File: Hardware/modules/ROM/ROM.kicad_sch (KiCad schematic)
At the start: 10 parts, among them J1 Bus_PCI_6502, U1 74HC138, U2 SST39SF040, U3 74HC00, U4 AS6C4008-55PCN

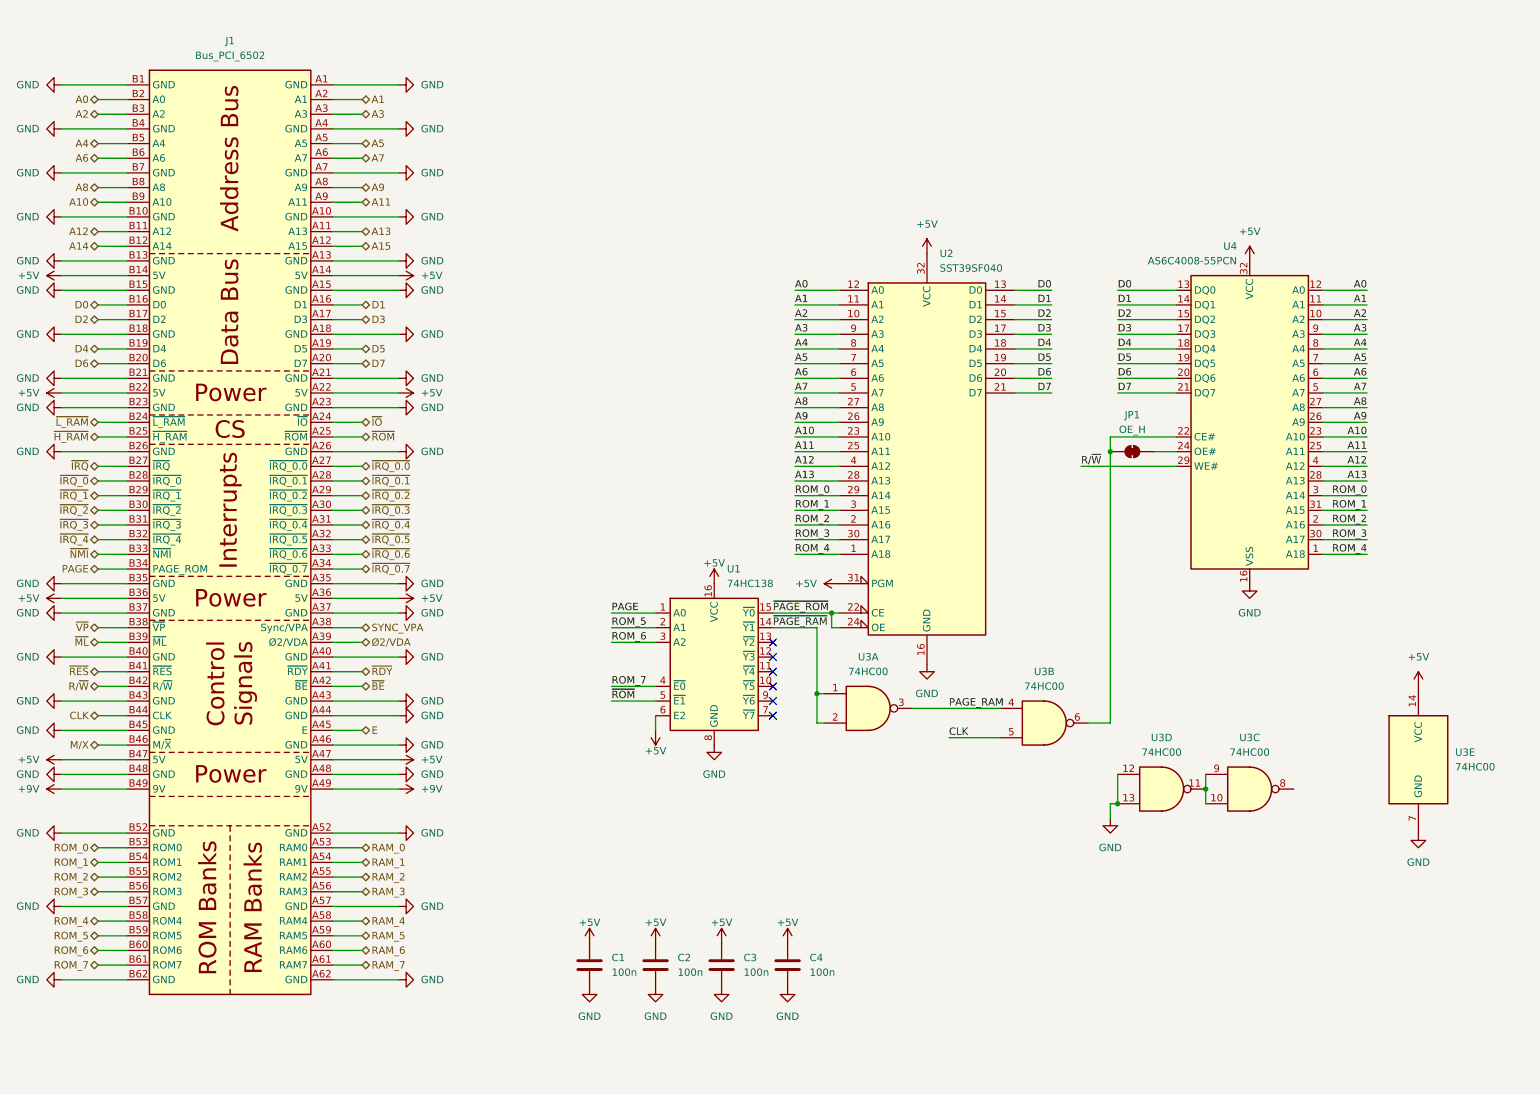
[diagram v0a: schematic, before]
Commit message: Hardware Update Add MyCPU VGA Module Beautify all Schematics minor Error corrections Readme Update
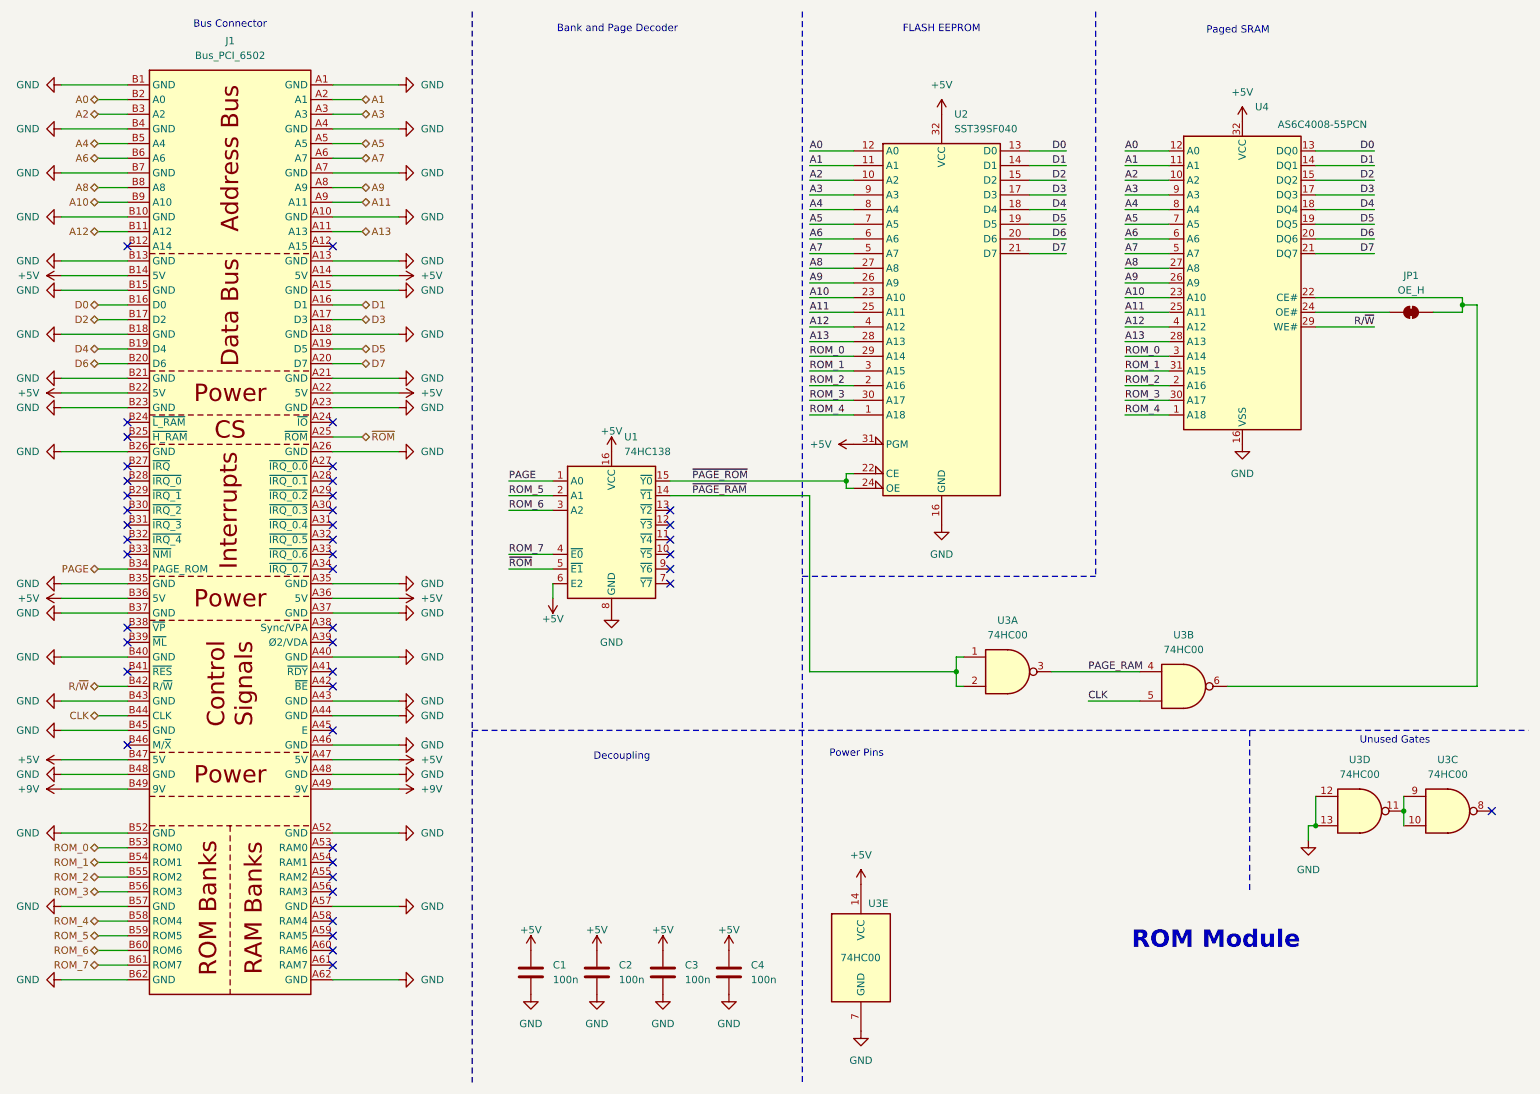
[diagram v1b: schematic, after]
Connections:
- net A14: no longer names the net of J1.B12 (A14)
- net A15: no longer names the net of J1.A12 (A15)
- net E: no longer names the net of J1.A45 (E)
- net M/X: no longer names the net of J1.B46 (M/~{X})
- net RAM_0: no longer names the net of J1.A53 (RAM0)
- net RAM_1: no longer names the net of J1.A54 (RAM1)
- net RAM_2: no longer names the net of J1.A55 (RAM2)
- net RAM_3: no longer names the net of J1.A56 (RAM3)
- net RAM_4: no longer names the net of J1.A58 (RAM4)
- net RAM_5: no longer names the net of J1.A59 (RAM5)
- net RAM_6: no longer names the net of J1.A60 (RAM6)
- net RAM_7: no longer names the net of J1.A61 (RAM7)
- net SYNC_VPA: no longer names the net of J1.A38 (Sync/VPA)
- net ~{BE}: no longer names the net of J1.A42 (~{BE})
- net ~{H_RAM}: no longer names the net of J1.B25 (~{H_RAM})
- net ~{IO}: no longer names the net of J1.A24 (~{IO})
- net ~{IRQ_0.0}: no longer names the net of J1.A27 (~{IRQ_0.0})
- net ~{IRQ_0.1}: no longer names the net of J1.A28 (~{IRQ_0.1})
- net ~{IRQ_0.2}: no longer names the net of J1.A29 (~{IRQ_0.2})
- net ~{IRQ_0.3}: no longer names the net of J1.A30 (~{IRQ_0.3})
- net ~{IRQ_0.4}: no longer names the net of J1.A31 (~{IRQ_0.4})
- net ~{IRQ_0.5}: no longer names the net of J1.A32 (~{IRQ_0.5})
- net ~{IRQ_0.6}: no longer names the net of J1.A33 (~{IRQ_0.6})
- net ~{IRQ_0.7}: no longer names the net of J1.A34 (~{IRQ_0.7})
- net ~{IRQ_0}: no longer names the net of J1.B28 (~{IRQ_0})
- net ~{IRQ_1}: no longer names the net of J1.B29 (~{IRQ_1})
- net ~{IRQ_2}: no longer names the net of J1.B30 (~{IRQ_2})
- net ~{IRQ_3}: no longer names the net of J1.B31 (~{IRQ_3})
- net ~{IRQ_4}: no longer names the net of J1.B32 (~{IRQ_4})
- net ~{IRQ}: no longer names the net of J1.B27 (~{IRQ})
- net ~{L_RAM}: no longer names the net of J1.B24 (~{L_RAM})
- net ~{ML}: no longer names the net of J1.B39 (~{ML})
- net ~{NMI}: no longer names the net of J1.B33 (~{NMI})
- net ~{RDY}: no longer names the net of J1.A41 (~{RDY})
- net ~{RES}: no longer names the net of J1.B41 (~{RES})
- net ~{VP}: no longer names the net of J1.B38 (~{VP})
- net Ø2/VDA: no longer names the net of J1.A39 (Ø2/VDA)
- no-connect marks 6 -> 44
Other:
- note added: "Bank and Page Decoder"
- note added: "Bus Connector"
- note added: "Decoupling"
- note added: "FLASH EEPROM"
- note added: "Paged SRAM"
- note added: "Power Pins"
- note added: "ROM Module"
- note added: "Unused Gates"
- company: (none) -> Synthron
- title: (none) -> S65xx Computer System
- moved on the sheet: C1, C2, C3, C4, JP1, U1, U2, U3A, U3B, U3C, U3D, U3E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

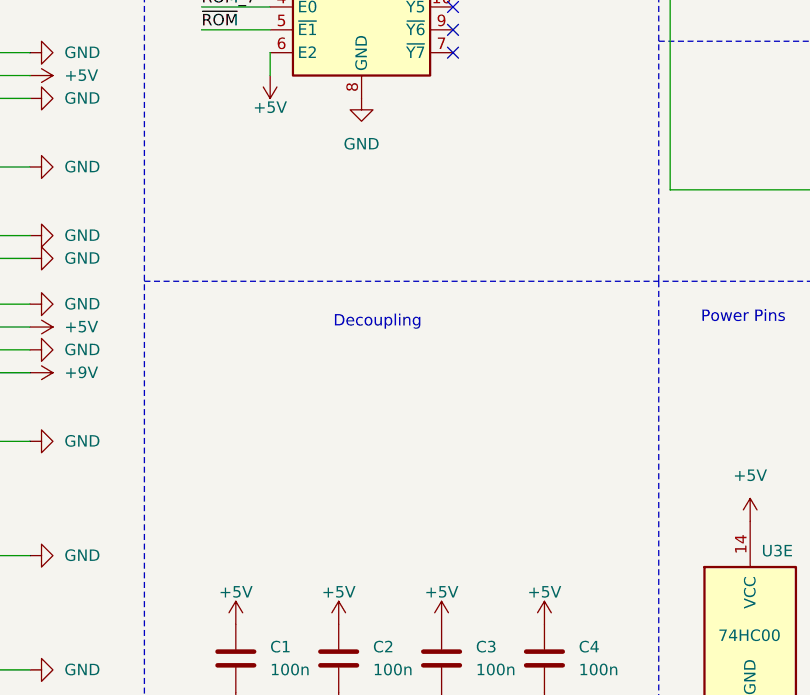
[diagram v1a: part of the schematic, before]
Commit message: Hardware Review Pt. 1 fix Address Decoding for Strobe Generators add bulk capacitance to every board fix wiring of Prototyping Board
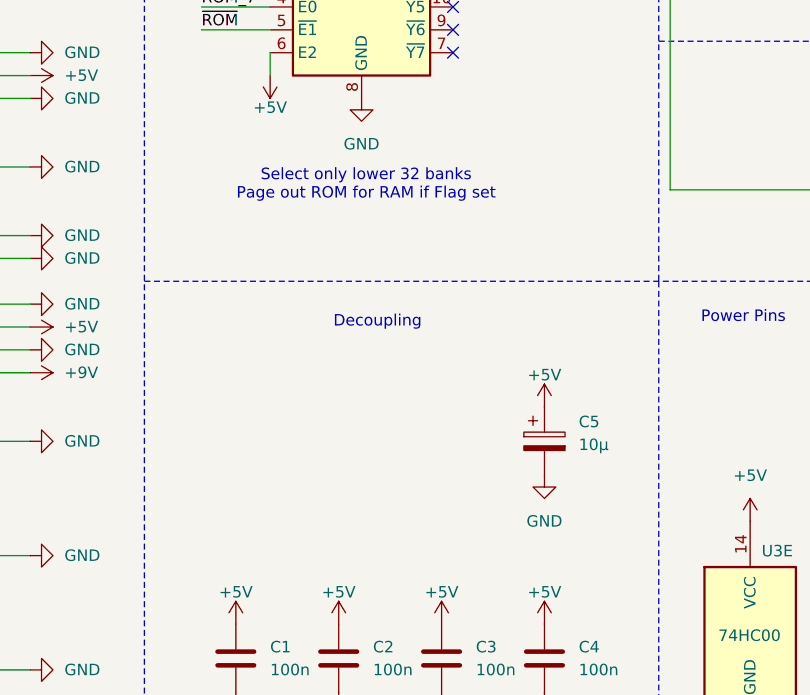
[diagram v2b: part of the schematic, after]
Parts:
- added C5: 10µ, Capacitor_THT:CP_Radial_D5.0mm_P2.50mm, symbol Device:C_Polarized
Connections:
- net +5V: now also C5.1
- net GND: now also C5.2
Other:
- note added: "Select only lower 32 banks Page out ROM for RAM if Flag set"
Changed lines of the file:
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@@
 		)
 	)
+	(text "Select only lower 32 banks\nPage out ROM for RAM if Flag set"
+		(exclude_from_sim no)
+		(at 126.238 126.492 0)
+		(effects
+			(font
+				(size 1.27 1.27)
+			)
+		)
+	)
 	(text "Bus Connector"
 		(exclude_from_sim no)
@@
 	)
 	(symbol
+		(lib_id "power:+5V")
+		(at 146.05 151.13 0)
+		(unit 1)
+		(exclude_from_sim no)
+		(in_bom yes)
+		(on_board yes)
+		(dnp no)
+		(property "Reference" "#PWR069"
+			(at 146.05 154.94 0)
+			(effects
+				(font
+					(size 1.27 1.27)
+				)
+				(hide yes)
+			)
+		)
+		(property "Value" "+5V"
+			(at 146.05 147.574 0)
+			(effects
+				(font
+					(size 1.27 1.27)
+				)
+			)
+		)
+		(property "Footprint" ""
+			(at 146.05 151.13 0)
+			(effects
+				(font
+					(size 1.27 1.27)
+				)
+				(hide yes)
+			)
+		)
+		(property "Datasheet" ""
+			(at 146.05 151.13 0)
+			(effects
+				(font
+					(size 1.27 1.27)
+				)
+				(hide yes)
+			)
+		)
+		(property "Description" "Power symbol creates a global label with name \"+5V\""
+			(at 146.05 151.13 0)
+			(effects
+				(font
+					(size 1.27 1.27)
+				)
+				(hide yes)
+			)
+		)
+		(pin "1"
+		)
+		(instances
+			(project "ROM"
+				(path "/24cc0665-6bb2-4c42-be07-61e5b80ca82f"
+					(reference "#PWR069")
+					(unit 1)
+				)
+			)
+		)
+	)
+	(symbol
 		(lib_id "Device:C")
 		(at 134.62 179.07 0)
@@
 	(symbol
 		(lib_id "power:GND")
+		(at 146.05 158.75 0)
+		(unit 1)
+		(exclude_from_sim no)
+		(in_bom yes)
+		(on_board yes)
+		(dnp no)
+		(fields_autoplaced yes)
+		(property "Reference" "#PWR070"
+			(at 146.05 165.1 0)
+			(effects
+				(font
+					(size 1.27 1.27)
+				)
+				(hide yes)
+			)
+		)
+		(property "Value" "GND"
+			(at 146.05 163.83 0)
+			(effects
+				(font
+					(size 1.27 1.27)
+				)
+			)
+		)
+		(property "Footprint" ""
+			(at 146.05 158.75 0)
+			(effects
+				(font
+					(size 1.27 1.27)
+				)
+				(hide yes)
+			)
+		)
+		(property "Datasheet" ""
+			(at 146.05 158.75 0)
+			(effects
+				(font
+					(size 1.27 1.27)
+				)
+				(hide yes)
+			)
+		)
+		(property "Description" "Power symbol creates a global label with name \"GND\" , ground"
+			(at 146.05 158.75 0)
+			(effects
+				(font
+					(size 1.27 1.27)
+				)
+				(hide yes)
+			)
+		)
+		(pin "1"
+		)
+		(instances
+			(project "ROM"
+				(path "/24cc0665-6bb2-4c42-be07-61e5b80ca82f"
+					(reference "#PWR070")
+					(unit 1)
+				)
+			)
+		)
+	)
+	(symbol
+		(lib_id "power:GND")
 		(at 88.9 132.08 90)
 		(mirror x)
@@
 					(unit 1)
 				)
+			)
+		)
+	)
+	(symbol
+		(lib_id "Device:C_Polarized")
+		(at 146.05 154.94 0)
+		(unit 1)
+		(exclude_from_sim no)
+		(in_bom yes)
+		(on_board yes)
+		(dnp no)
+		(fields_autoplaced yes)
+		(property "Reference" "C5"
+			(at 149.86 152.7809 0)
+			(effects
+				(font
+					(size 1.27 1.27)
+				)
+				(justify left)
+			)
+		)
+		(property "Value" "10µ"
+			(at 149.86 155.3209 0)
+			(effects
+				(font
+					(size 1.27 1.27)
+				)
+				(justify left)
+			)
+		)
+		(property "Footprint" "Capacitor_THT:CP_Radial_D5.0mm_P2.50mm"
+			(at 147.0152 158.75 0)
+			(effects
+				(font
+					(size 1.27 1.27)
+				)
+				(hide yes)
+			)
+		)
+		(property "Datasheet" "~"
+			(at 146.05 154.94 0)
+			(effects
+				(font
+					(size 1.27 1.27)
+				)
+				(hide yes)
+			)
+		)
+		(property "Description" "Polarized capacitor"
+			(at 146.05 154.94 0)
+			(effects
+				(font
+					(size 1.27 1.27)
+				)
+				(hide yes)
+			)
+		)
+		(pin "1"
+		)
+		(pin "2"
+		)
+		(instances
+			(project ""
+				(path "/24cc0665-6bb2-4c42-be07-61e5b80ca82f"
+					(reference "C5")
+					(unit 1)
+				)
